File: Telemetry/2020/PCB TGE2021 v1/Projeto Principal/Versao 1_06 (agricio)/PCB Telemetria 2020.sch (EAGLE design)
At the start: 53 parts, among them IC1 INA240A1DR, IC2 MCP3221A6T-E_OTVAO, IC3 AZ1117IH-3.3TRG1, IC4 ACS758LCB-050B-PFF-T, IC5 ADS1115IDGSR, IC6 ACS712-030B3, IC7 THVD2410DR, J1 172042-0406, U1 TMP100NA/3K

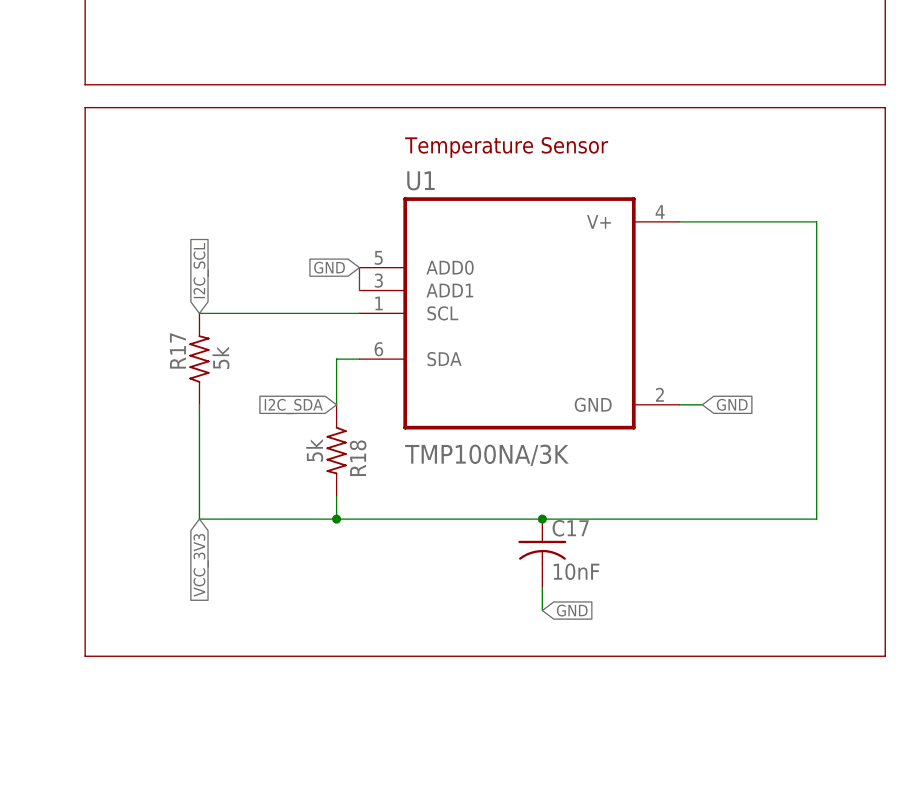
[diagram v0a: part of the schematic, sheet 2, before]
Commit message: Adicao do sensor de temperetura ao esquemático
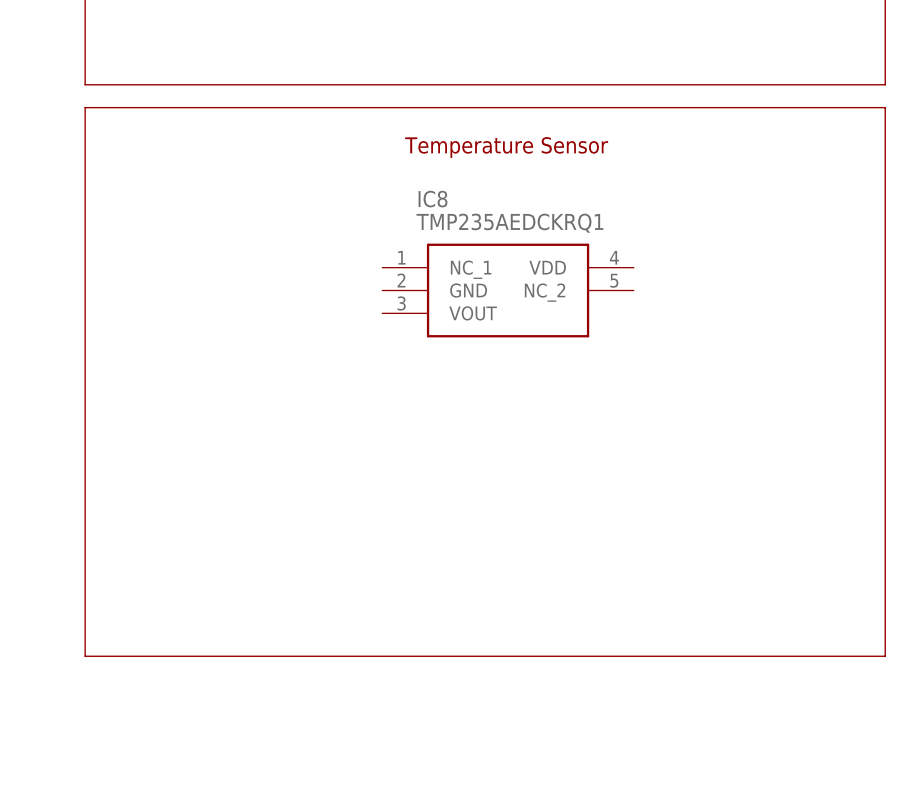
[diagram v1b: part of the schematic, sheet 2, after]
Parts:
- removed C17: 10nF, rcl:C-USC0805
- removed R17, R18: 5k, rcl:R-US_R0805
- removed U1: TMP100NA/3K, TMP100NA_3K:TMP100NA/3K
- added IC8: TMP235AEDCKRQ1, SamacSys_Parts:TMP235AEDCKRQ1
- added J2, J3, J4, J5: 43045-0412, SamacSys_Parts:43045-0412
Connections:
- net GND: no longer C17.2, U1.ADD0, U1.ADD1, U1.GND
- net I2C_SCL: no longer R17.2, U1.SCL
- net I2C_SDA: no longer R18.1, U1.SDA
- net VCC_3V3: no longer C17.1, R17.1, R18.2, U1.V+
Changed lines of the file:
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@@
 <part name="SUPPLY5" library="supply2" library_urn="urn:adsk.eagle:library:372" deviceset="GND" device=""/>
 <part name="SUPPLY6" library="supply2" library_urn="urn:adsk.eagle:library:372" deviceset="GND" device=""/>
-<part name="U1" library="TMP100NA_3K" deviceset="TMP100NA/3K" device=""/>
-<part name="R17" library="rcl" library_urn="urn:adsk.eagle:library:334" deviceset="R-US_" device="R0805" package3d_urn="urn:adsk.eagle:package:23553/2" value="5k"/>
-<part name="R18" library="rcl" library_urn="urn:adsk.eagle:library:334" deviceset="R-US_" device="R0805" package3d_urn="urn:adsk.eagle:package:23553/2" value="5k"/>
-<part name="C17" library="rcl" library_urn="urn:adsk.eagle:library:334" deviceset="C-US" device="C0805" package3d_urn="urn:adsk.eagle:package:23617/2" value="10nF"/>
 <part name="FRAME5" library="frames" library_urn="urn:adsk.eagle:library:229" deviceset="A3L-LOC" device=""/>
+<part name="J2" library="SamacSys_Parts" deviceset="43045-0412" device=""/>
+<part name="J3" library="SamacSys_Parts" deviceset="43045-0412" device=""/>
+<part name="J4" library="SamacSys_Parts" deviceset="43045-0412" device=""/>
+<part name="J5" library="SamacSys_Parts" deviceset="43045-0412" device=""/>
+<part name="IC8" library="SamacSys_Parts" deviceset="TMP235AEDCKRQ1" device=""/>
 </parts>
 <sheets>
@@
 <attribute name="VALUE" x="330.962" y="166.37" size="1.778" layer="96" rot="R90"/>
 </instance>
-<instance part="U1" gate="A" x="332.74" y="119.38" smashed="yes">
-<attribute name="NAME" x="320.04" y="133.08" size="2.0828" layer="95" ratio="10" rot="SR0"/>
-<attribute name="VALUE" x="320.04" y="102.68" size="2.0828" layer="96" ratio="10" rot="SR0"/>
-</instance>
-<instance part="R17" gate="G$1" x="297.18" y="114.3" smashed="yes" rot="R90">
-<attribute name="NAME" x="295.6814" y="113.03" size="1.778" layer="95" rot="R90"/>
-<attribute name="VALUE" x="300.482" y="113.03" size="1.778" layer="96" rot="R90"/>
-</instance>
-<instance part="R18" gate="G$1" x="312.42" y="104.14" smashed="yes" rot="R270">
-<attribute name="NAME" x="313.9186" y="105.41" size="1.778" layer="95" rot="R270"/>
-<attribute name="VALUE" x="309.118" y="105.41" size="1.778" layer="96" rot="R270"/>
-</instance>
-<instance part="C17" gate="G$1" x="335.28" y="93.98" smashed="yes">
-<attribute name="NAME" x="336.296" y="94.615" size="1.778" layer="95"/>
-<attribute name="VALUE" x="336.296" y="89.789" size="1.778" layer="96"/>
+<instance part="IC8" gate="G$1" x="317.5" y="124.46" smashed="yes">
+<attribute name="NAME" x="321.31" y="132.08" size="1.778" layer="95" align="center-left"/>
+<attribute name="VALUE" x="321.31" y="129.54" size="1.778" layer="96" align="center-left"/>
 </instance>
 </instances>
@@
 <wire x1="347.98" y1="160.02" x2="347.98" y2="162.56" width="0.1524" layer="91"/>
 </segment>
-<segment>
-<pinref part="U1" gate="A" pin="ADD0"/>
-<pinref part="U1" gate="A" pin="ADD1"/>
-<wire x1="314.96" y1="124.46" x2="314.96" y2="121.92" width="0.1524" layer="91"/>
-<label x="314.96" y="124.46" size="1.27" layer="95" rot="R180" xref="yes"/>
-</segment>
-<segment>
-<pinref part="U1" gate="A" pin="GND"/>
-<wire x1="350.52" y1="109.22" x2="353.06" y2="109.22" width="0.1524" layer="91"/>
-<label x="353.06" y="109.22" size="1.27" layer="95" xref="yes"/>
-</segment>
-<segment>
-<pinref part="C17" gate="G$1" pin="2"/>
-<wire x1="335.28" y1="88.9" x2="335.28" y2="86.36" width="0.1524" layer="91"/>
-<label x="335.28" y="86.36" size="1.27" layer="95" xref="yes"/>
-</segment>
 </net>
 <net name="VCC_3V3" class="0">
@@
 <wire x1="327.66" y1="157.48" x2="322.58" y2="157.48" width="0.1524" layer="91"/>
 </segment>
-<segment>
-<pinref part="R18" gate="G$1" pin="2"/>
-<pinref part="C17" gate="G$1" pin="1"/>
-<wire x1="312.42" y1="99.06" x2="312.42" y2="96.52" width="0.1524" layer="91"/>
-<wire x1="312.42" y1="96.52" x2="335.28" y2="96.52" width="0.1524" layer="91"/>
-<pinref part="R17" gate="G$1" pin="1"/>
-<wire x1="297.18" y1="109.22" x2="297.18" y2="96.52" width="0.1524" layer="91"/>
-<wire x1="297.18" y1="96.52" x2="312.42" y2="96.52" width="0.1524" layer="91"/>
-<junction x="312.42" y="96.52"/>
-<pinref part="U1" gate="A" pin="V+"/>
-<wire x1="350.52" y1="129.54" x2="365.76" y2="129.54" width="0.1524" layer="91"/>
-<wire x1="365.76" y1="129.54" x2="365.76" y2="96.52" width="0.1524" layer="91"/>
-<wire x1="365.76" y1="96.52" x2="335.28" y2="96.52" width="0.1524" layer="91"/>
-<junction x="335.28" y="96.52"/>
-<label x="297.18" y="96.52" size="1.27" layer="95" rot="R270" xref="yes"/>
-</segment>
 </net>
 <net name="MSHUNT_AMP" class="0">
@@
 <label x="76.2" y="200.66" size="1.27" layer="95" rot="R90" xref="yes"/>
 </segment>
-<segment>
-<pinref part="R18" gate="G$1" pin="1"/>
-<pinref part="U1" gate="A" pin="SDA"/>
-<wire x1="312.42" y1="109.22" x2="312.42" y2="114.3" width="0.1524" layer="91"/>
-<wire x1="312.42" y1="114.3" x2="314.96" y2="114.3" width="0.1524" layer="91"/>
-<label x="312.42" y="109.22" size="1.27" layer="95" rot="R180" xref="yes"/>
-</segment>
 </net>
 <net name="I2C_SCL" class="0">
@@
 <wire x1="73.66" y1="195.58" x2="73.66" y2="200.66" width="0.1524" layer="91"/>
 <label x="73.66" y="200.66" size="1.27" layer="95" rot="R90" xref="yes"/>
-</segment>
-<segment>
-<pinref part="R17" gate="G$1" pin="2"/>
-<pinref part="U1" gate="A" pin="SCL"/>
-<wire x1="297.18" y1="119.38" x2="314.96" y2="119.38" width="0.1524" layer="91"/>
-<label x="297.18" y="119.38" size="1.27" layer="95" rot="R90" xref="yes"/>
 </segment>
 </net>
@@
 <attribute name="SHEET" x="357.505" y="5.08" size="2.54" layer="94"/>
 </instance>
+<instance part="J2" gate="G$1" x="15.24" y="246.38" smashed="yes">
+<attribute name="NAME" x="31.75" y="254" size="1.778" layer="95" align="center-left"/>
+<attribute name="VALUE" x="31.75" y="251.46" size="1.778" layer="96" align="center-left"/>
+</instance>
+<instance part="J3" gate="G$1" x="15.24" y="236.22" smashed="yes">
+<attribute name="NAME" x="31.75" y="243.84" size="1.778" layer="95" align="center-left"/>
+<attribute name="VALUE" x="31.75" y="241.3" size="1.778" layer="96" align="center-left"/>
+</instance>
+<instance part="J4" gate="G$1" x="15.24" y="226.06" smashed="yes">
+<attribute name="NAME" x="31.75" y="233.68" size="1.778" layer="95" align="center-left"/>
+<attribute name="VALUE" x="31.75" y="231.14" size="1.778" layer="96" align="center-left"/>
+</instance>
+<instance part="J5" gate="G$1" x="15.24" y="215.9" smashed="yes">
+<attribute name="NAME" x="31.75" y="223.52" size="1.778" layer="95" align="center-left"/>
+<attribute name="VALUE" x="31.75" y="220.98" size="1.778" layer="96" align="center-left"/>
+</instance>
 </instances>
